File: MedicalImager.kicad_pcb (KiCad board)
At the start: 2 copper layers, 513 parts, among them J1001 TYPE-C-31-M-12, J1002 B8B-XH-A, J1003 External Board 1, J1004 External Board 2, J1005 47352-1001, J501 REF-226081-01, J502 REF-226081-01, Q1001 SI2302DS, Q1401 FDMC86240, Q1601 FDMC86240, SW501 RESET, U1001 NXB0108BQ-Q100X, U1002 USBLC6-2SC6, U1003 TUSB1210BRHBR, U1004 NXB0104PWJ, U1005 NVT4858HKZ, U1101 TPS54302, U1301 TPS54302, U1401 LM5155DSSR, U1501 TPS54302, U1601 LM5155DSSR, U1701 TPS54302, U1801 TPS54302, U1901 TPS51385RJNR, U2001 TPS51385RJNR, U301 LMK1D1204RGTR, U302 LMK1D1204RGTR, U401 TPS63700DRCR, U402 NCP176BMX180TCG, U403 NCP176AMX330TCG, U404 NCP176BMX180TCG, U405 NCP176AMX330TCG, U406 NCP176BMX180TCG, U407 MIC5363-3.3YMT-TR, U408 NCP176AMX330TCG, U410 TPS22918TDBVRQ1, U601 AD8285WBCPZ, U701 AD8285WBCPZ, U801 AD8285WBCPZ, U901 AD8285WBCPZ, Y301 ASFLMB-72.000MHZ-LY-T

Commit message: finished preliminary placement, will definietly be changed when routing don't forget to apply comments in first page and calculate trace impedance for all traces & make AI revise schematic
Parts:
- removed C308, C325: 100nF, Capacitor_SMD:C_0402_1005Metric
- removed C326: 10uF, Capacitor_SMD:C_0402_1005Metric
- added C1019: 100nF, Capacitor_SMD:C_0402_1005Metric, B.Cu at (124.5, 162.1)
- added R1008: 50R, Resistor_SMD:R_0402_1005Metric, B.Cu at (127.4, 158.1)
- added Y1001: TG-5006CG-12H_26.0000M3, TG-5006CG-12H 26.0000M3:TG5006CG12H260000M3, B.Cu at (124.2, 159.2)
- C1001, C1002, C1016, C1017, R402: moved to F.Cu
- C1004, C1005, C1008, C1011, C1013, C1101, C1102, C1103, C1104, C1105, C1301, C1302, C1303, C1304, C1305, C1306, C1401, C1402, C1403, C1404, C1405, C1406, C1407, C1408, C1409, C1410, C1411, C1501, C1502, C1503, C1504, C1505, C1601, C1602, C1603, C1604, C1605, C1606, C1607, C1608, C1609, C1610, C1611, C1701, C1702, C1703, C1704, C1705, C1706, C1801, C1802, C1803, C1804, C1805, C1901, C1902, C1903, C1904, C1905, C1906, C1907, C1908, C1909, C1910, C2001, C2002, C2003, C2004, C2005, C2006, C2007, C2008, C2009, C2010, C301, C302, C303, C305, C306, C309, C310, C312, C314, C315, C317, C319, C321, C323, C324, C327, C401, C402, C403, C404, C405, C406, C407, C408, C409, C410, C411, C415, C416, C419, C420, C421, C501, C502, C503, C504, C505, C506, C507, C508, C509, C510, C511, C513, C514, C515, C516, C517, C518, C519, C520, C521, D1401, D1402, D1601, D1602, D408, F1001, J1001, J1002, J1003, J1004, J1005, JP1401, JP1402, JP1601, JP1602, JP401, JP402, JP403, JP404, JP405, JP406, JP407, JP408, JP409, JP501, JP502, JP503, JP504, L1101, L1301, L1401, L1402, L1403, L1404, L1405, L1501, L1601, L1602, L1603, L1604, L1605, L1701, L1801, L1901, L2001, L401, Q1001, Q1401, Q1601, R1001, R1002, R1003, R1004, R1005, R1006, R1007, R1101, R1102, R1301, R1302, R1401, R1402, R1403, R1404, R1405, R1406, R1501, R1502, R1601, R1602, R1603, R1604, R1605, R1606, R1701, R1702, R1801, R1802, R1901, R1902, R1903, R1904, R1905, R2001, R2002, R2003, R2004, R2005, R301, R302, R303, R304, R305, R306, R404, R410, R411, R413, R416, R417, R418, R419, R420, R421, U1001, U1002, U1003, U1004, U1101, U1301, U1401, U1501, U1601, U1701, U1801, U1901, U2001, U301, U302, U401, U402, U403, U404, U405, U406, U407, U410, Y301: moved to B.Cu
- SW501: footprint Button_Switch_SMD:Nidec_Copal_CAS-120A -> Button_Switch_SMD:SW_Push_SPST_NO_Alps_SKRK
- moved R416 361.4 mm to (80.6, 93.0)
- moved R417 347.7 mm to (84.7, 93.0)
- moved J502 340.4 mm to (66.8, 129.2), turned to 90 degrees
- moved C407 328.5 mm to (117.4, 93.0)
- moved U402 325.6 mm to (118.9, 93.0)
- moved C303 325.4 mm to (119.0, 91.5), turned to 0 degrees
- moved C310 325.4 mm to (119.0, 90.5), turned to 0 degrees
- moved C408 321.8 mm to (114.4, 93.0)
- moved C617 320.8 mm to (120.0, 87.7)
- moved C620 320.8 mm to (120.0, 86.7)
- moved C601 320.8 mm to (124.8, 82.6)
- moved C602 320.8 mm to (131.7, 83.1)
- moved C603 320.8 mm to (131.2, 90.9)
- moved C604 320.8 mm to (123.1, 83.8)
- moved C605 320.8 mm to (130.2, 82.6)
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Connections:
- net /Interface/USB_CLK renamed /Interface/USB_SOM_CLK
- C618 pad 1: /RX/CLKOUT_A0_N -> /RX/CLKOUT_B1_N
- C619 pad 1: /RX/CLKOUT_A0_P -> /RX/CLKOUT_B1_P
- C718 pad 1: /RX/CLKOUT_A1_N -> /RX/CLKOUT_B0_N
- C719 pad 1: /RX/CLKOUT_A1_P -> /RX/CLKOUT_B0_P
- C818 pad 1: /RX/CLKOUT_B0_N -> /RX/CLKOUT_A1_N
- C819 pad 1: /RX/CLKOUT_B0_P -> /RX/CLKOUT_A1_P
- C918 pad 1: /RX/CLKOUT_B1_N -> /RX/CLKOUT_A0_N
- C919 pad 1: /RX/CLKOUT_B1_P -> /RX/CLKOUT_A0_P
- J501 pad B32: /SOM/LCD_POWER -> /Interface/LCD_POWER
- J501 pad B33: /SOM/LCD_TX_MAIN -> /Interface/LCD_TX_MAIN
- J501 pad B34: /SOM/LCD_RX_MAIN -> /Interface/LCD_RX_MAIN
- J502 pad A46: /RX/AFE_OUTPUTS3 -> /RX/AFE_OUTPUTS15
- J502 pad A47: /RX/AFE_OUTPUTS4 -> /RX/AFE_OUTPUTS16
- J502 pad A48: /RX/AFE_OUTPUTS5 -> /RX/AFE_OUTPUTS17
- J502 pad A50: /RX/AFE_OUTPUTS9 -> /RX/AFE_OUTPUTS21
- J502 pad A51: /RX/AFE_OUTPUTS10 -> /RX/AFE_OUTPUTS22
- J502 pad A52: /RX/AFE_OUTPUTS11 -> /RX/AFE_OUTPUTS23
- J502 pad A54: /RX/AFE_OUTPUTS15 -> /RX/AFE_OUTPUTS39
- J502 pad A55: /RX/AFE_OUTPUTS16 -> /RX/AFE_OUTPUTS40
- J502 pad A56: /RX/AFE_OUTPUTS17 -> /RX/AFE_OUTPUTS41
- J502 pad A58: /RX/AFE_OUTPUTS21 -> /RX/AFE_OUTPUTS45
- J502 pad A59: /RX/AFE_OUTPUTS22 -> /RX/AFE_OUTPUTS46
- J502 pad A60: /RX/AFE_OUTPUTS23 -> /RX/AFE_OUTPUTS47
- J502 pad B44: /RX/AFE_OUTPUTS0 -> /RX/AFE_OUTPUTS12
- J502 pad B45: /RX/AFE_OUTPUTS1 -> /RX/AFE_OUTPUTS13
- J502 pad B46: /RX/AFE_OUTPUTS2 -> /RX/AFE_OUTPUTS14
- J502 pad B48: /RX/AFE_OUTPUTS6 -> /RX/AFE_OUTPUTS18
- J502 pad B49: /RX/AFE_OUTPUTS7 -> /RX/AFE_OUTPUTS19
- J502 pad B50: /RX/AFE_OUTPUTS8 -> /RX/AFE_OUTPUTS20
- J502 pad B52: /RX/AFE_OUTPUTS12 -> /RX/AFE_OUTPUTS36
- J502 pad B53: /RX/AFE_OUTPUTS13 -> /RX/AFE_OUTPUTS37
- J502 pad B54: /RX/AFE_OUTPUTS14 -> /RX/AFE_OUTPUTS38
- J502 pad B56: /RX/AFE_OUTPUTS18 -> /RX/AFE_OUTPUTS42
- J502 pad B57: /RX/AFE_OUTPUTS19 -> /RX/AFE_OUTPUTS43
- J502 pad B58: /RX/AFE_OUTPUTS20 -> /RX/AFE_OUTPUTS44
- J502 pad C46: /RX/AFE_OUTPUTS27 -> /RX/AFE_OUTPUTS3
- J502 pad C47: /RX/AFE_OUTPUTS28 -> /RX/AFE_OUTPUTS4
- J502 pad C48: /RX/AFE_OUTPUTS29 -> /RX/AFE_OUTPUTS5
- J502 pad C50: /RX/AFE_OUTPUTS33 -> /RX/AFE_OUTPUTS9
- J502 pad C51: /RX/AFE_OUTPUTS34 -> /RX/AFE_OUTPUTS10
- J502 pad C52: /RX/AFE_OUTPUTS35 -> /RX/AFE_OUTPUTS11
- J502 pad C54: /RX/AFE_OUTPUTS39 -> /RX/AFE_OUTPUTS27
- J502 pad C55: /RX/AFE_OUTPUTS40 -> /RX/AFE_OUTPUTS28
- J502 pad C56: /RX/AFE_OUTPUTS41 -> /RX/AFE_OUTPUTS29
- J502 pad C58: /RX/AFE_OUTPUTS45 -> /RX/AFE_OUTPUTS33
- J502 pad C59: /RX/AFE_OUTPUTS46 -> /RX/AFE_OUTPUTS34
- J502 pad C60: /RX/AFE_OUTPUTS47 -> /RX/AFE_OUTPUTS35
- J502 pad D44: /RX/AFE_OUTPUTS24 -> /RX/AFE_OUTPUTS0
- J502 pad D45: /RX/AFE_OUTPUTS25 -> /RX/AFE_OUTPUTS1
- J502 pad D46: /RX/AFE_OUTPUTS26 -> /RX/AFE_OUTPUTS2
- J502 pad D48: /RX/AFE_OUTPUTS30 -> /RX/AFE_OUTPUTS6
- J502 pad D49: /RX/AFE_OUTPUTS31 -> /RX/AFE_OUTPUTS7
- J502 pad D50: /RX/AFE_OUTPUTS32 -> /RX/AFE_OUTPUTS8
- J502 pad D52: /RX/AFE_OUTPUTS36 -> /RX/AFE_OUTPUTS24
- J502 pad D53: /RX/AFE_OUTPUTS37 -> /RX/AFE_OUTPUTS25
- J502 pad D54: /RX/AFE_OUTPUTS38 -> /RX/AFE_OUTPUTS26
- J502 pad D56: /RX/AFE_OUTPUTS42 -> /RX/AFE_OUTPUTS30
- J502 pad D57: /RX/AFE_OUTPUTS43 -> /RX/AFE_OUTPUTS31
- J502 pad D58: /RX/AFE_OUTPUTS44 -> /RX/AFE_OUTPUTS32
- R1405 pad 1: PULSER_100V -> PULSER_50V_PRE
- R1605 pad 1: PULSER_100V -> PULSER_100V_PRE
- R603 pad 1: /RX/CLKOUT_A0_N -> /RX/CLKOUT_B1_N
- R603 pad 2: /RX/CLKOUT_A0_P -> /RX/CLKOUT_B1_P
- R703 pad 1: /RX/CLKOUT_A1_N -> /RX/CLKOUT_B0_N
- R703 pad 2: /RX/CLKOUT_A1_P -> /RX/CLKOUT_B0_P
- R803 pad 1: /RX/CLKOUT_B0_N -> /RX/CLKOUT_A1_N
- R803 pad 2: /RX/CLKOUT_B0_P -> /RX/CLKOUT_A1_P
- R903 pad 1: /RX/CLKOUT_B1_N -> /RX/CLKOUT_A0_N
- R903 pad 2: /RX/CLKOUT_B1_P -> /RX/CLKOUT_A0_P
- U1003 pad 1: GND -> /Interface/USB_REFCLK
- U1003 pad 18: /Interface/USB_PRE_P -> /Interface/USB_PRE_N
- U1003 pad 19: /Interface/USB_PRE_N -> /Interface/USB_PRE_P
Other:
- board outline added: 100 x 140 mm

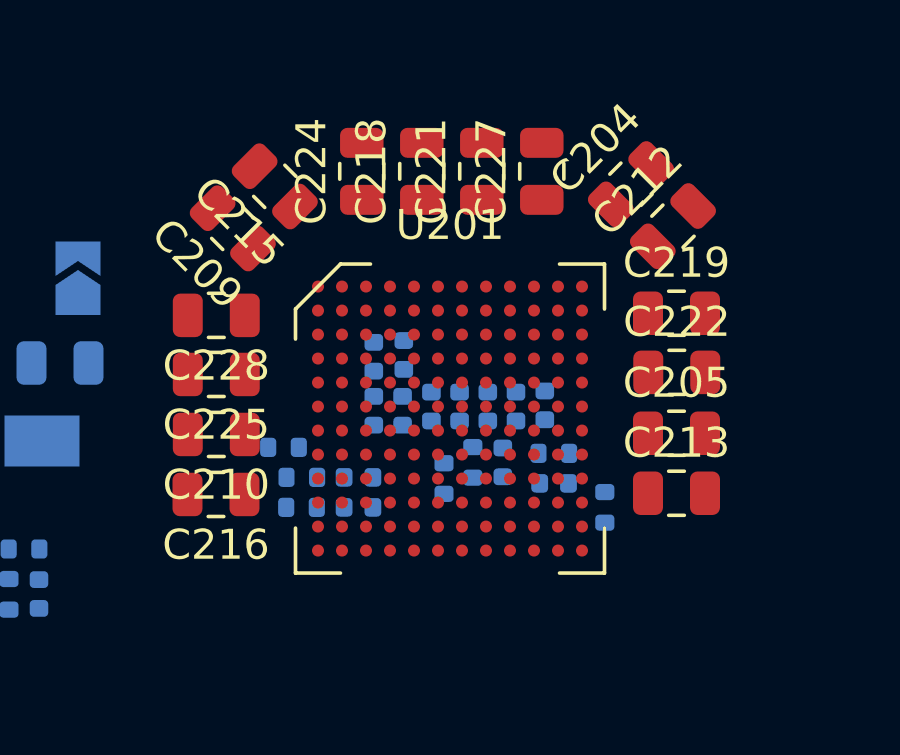
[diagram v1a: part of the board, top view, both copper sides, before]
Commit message: calculated impedances and started and almost finished fanout, needs revision
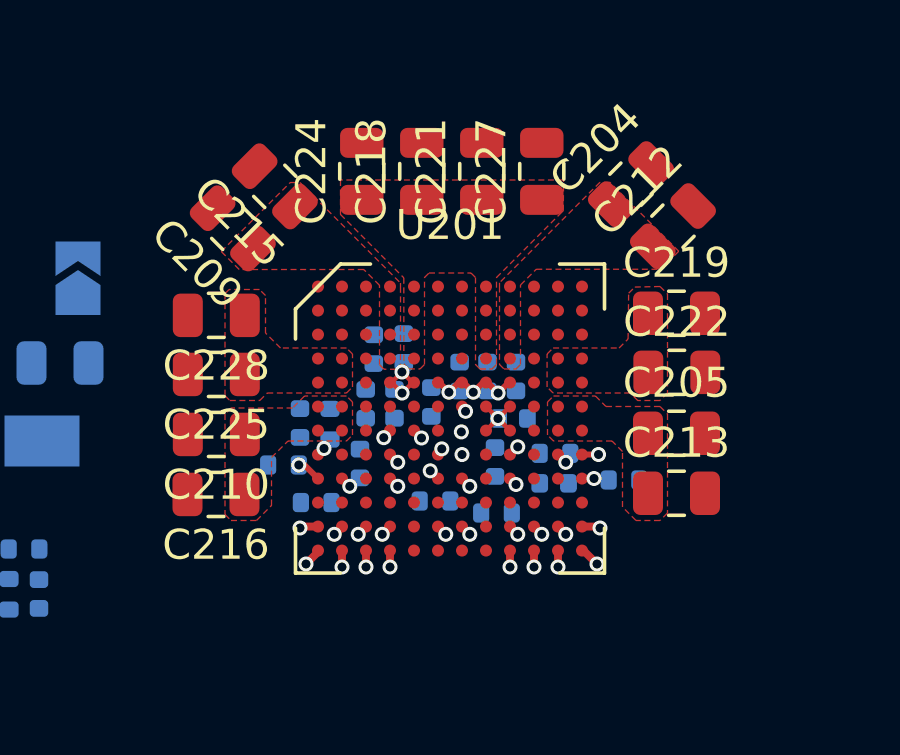
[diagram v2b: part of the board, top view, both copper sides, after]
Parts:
- moved C202 2.66 mm to (96.6, 60.6), turned to 90 degrees
- moved R206 2.01 mm to (97.6, 60.6), turned to 90 degrees
- moved R202 1.86 mm to (103.2, 63.6), turned to 180 degrees
- moved C203 1.46 mm to (98.6, 62.0), turned to 90 degrees
- moved C207 1.15 mm to (103.7, 60.5), turned to 0 degrees
- moved R203 1.11 mm to (107.4, 62.5), turned to 0 degrees
- moved C214 1.00 mm to (102.8, 59.0), turned to 90 degrees
- moved C217 1.00 mm to (103.8, 59.0), turned to 90 degrees
- moved C211 1.00 mm to (101.9, 59.1), turned to 90 degrees
- moved R205 0.81 mm to (101.1, 63.2), turned to 180 degrees
- moved R201 0.59 mm to (96.0, 62.0)
- moved R207 0.52 mm to (97.1, 63.3)
- moved C220 0.36 mm to (99.8, 60.0)
- moved C229 0.36 mm to (98.8, 60.0)
- moved C208 0.26 mm to (103.1, 61.9)
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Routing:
- net IM_5V: track 0.00 -> 3.22 mm, vias 0 -> 3
- net PULSER_1V8: track 0.00 -> 2.26 mm, vias 0 -> 1
- net PULSER_5VN: track 0.00 -> 2.18 mm, vias 0 -> 2
- net /SOM/PULSER_RESET: track 0.00 -> 0.83 mm, vias 0 -> 1
- net /RX/TR_OUT1: track 0.00 -> 0.69 mm, vias 0 -> 1
- net /RX/TR_OUT14: track 0.00 -> 0.62 mm, vias 0 -> 1
- net /RX/TR_OUT0: track 0.00 -> 0.62 mm, vias 0 -> 1
- net /RX/TR_OUT15: track 0.00 -> 0.61 mm, vias 0 -> 1
- net /SOM/PULSER_SPI_SDOUT: track 0.00 -> 0.55 mm, vias 0 -> 1
- net /RX/TR_OUT9: track 0.00 -> 0.55 mm, vias 0 -> 1
- net /RX/TR_OUT7: track 0.00 -> 0.55 mm, vias 0 -> 1
- net /RX/TR_OUT5: track 0.00 -> 0.55 mm, vias 0 -> 1
- net /RX/TR_OUT3: track 0.00 -> 0.55 mm, vias 0 -> 1
- net /RX/TR_OUT13: track 0.00 -> 0.55 mm, vias 0 -> 1
- net /RX/TR_OUT11: track 0.00 -> 0.55 mm, vias 0 -> 1
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- added copper zone on F.Cu, net PULSER_100V
- added copper zone on F.Cu, net PULSER_100VN
- added copper zone on F.Cu, net PULSER_50V
- added copper zone on F.Cu, net PULSER_50VN
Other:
- copper layers 2 -> 6
